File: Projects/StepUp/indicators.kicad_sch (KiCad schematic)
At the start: 10 parts, among them Q5 BSS83P

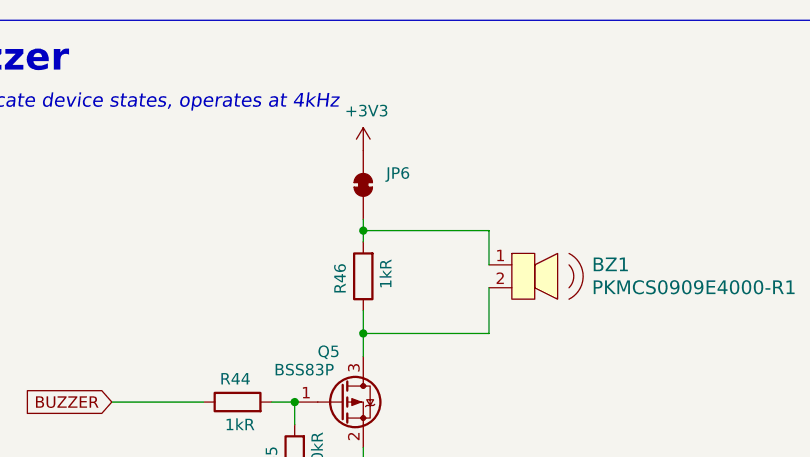
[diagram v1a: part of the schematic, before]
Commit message: feat(layout): DRC ongoing, layout nearly complete
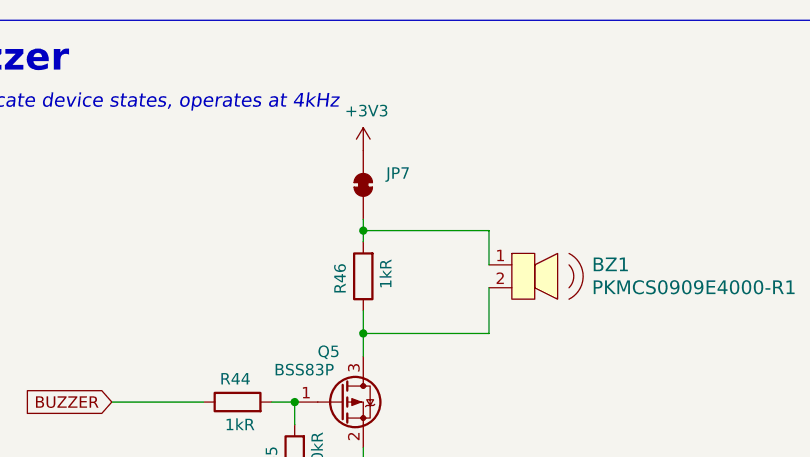
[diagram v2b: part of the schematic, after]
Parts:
- renumbered JP6 to JP7
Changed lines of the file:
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@@
 		(on_board yes)
 		(dnp no)
-		(property "Reference" "#PWR095"
+		(property "Reference" "#PWR0107"
 			(at 71.12 110.49 0)
 			(effects
@@
 			(project "StepUp"
 				(path "/e0cca1c7-c263-49eb-8c40-74000ebe5285/9dda156e-3fdf-45bb-95f8-ac79c3ca0e44"
-					(reference "#PWR095")
+					(reference "#PWR0107")
 					(unit 1)
 				)
@@
 		(on_board yes)
 		(dnp no)
-		(property "Reference" "#PWR097"
+		(property "Reference" "#PWR0109"
 			(at 200.66 77.47 0)
 			(effects
@@
 			(project "StepUp"
 				(path "/e0cca1c7-c263-49eb-8c40-74000ebe5285/9dda156e-3fdf-45bb-95f8-ac79c3ca0e44"
-					(reference "#PWR097")
+					(reference "#PWR0109")
 					(unit 1)
 				)
@@
 		(on_board yes)
 		(dnp no)
-		(property "Reference" "#PWR096"
+		(property "Reference" "#PWR0108"
 			(at 193.04 120.65 0)
 			(effects
@@
 			(project "StepUp"
 				(path "/e0cca1c7-c263-49eb-8c40-74000ebe5285/9dda156e-3fdf-45bb-95f8-ac79c3ca0e44"
-					(reference "#PWR096")
+					(reference "#PWR0108")
 					(unit 1)
 				)
@@
 		(dnp no)
 		(fields_autoplaced yes)
-		(property "Reference" "JP6"
+		(property "Reference" "JP7"
 			(at 203.2 76.1999 90)
 			(effects
@@
 			(project "StepUp"
 				(path "/e0cca1c7-c263-49eb-8c40-74000ebe5285/9dda156e-3fdf-45bb-95f8-ac79c3ca0e44"
-					(reference "JP6")
+					(reference "JP7")
 					(unit 1)
 				)
@@
 		(on_board yes)
 		(dnp no)
-		(property "Reference" "#PWR098"
+		(property "Reference" "#PWR0110"
 			(at 200.66 120.65 0)
 			(effects
@@
 			(project "StepUp"
 				(path "/e0cca1c7-c263-49eb-8c40-74000ebe5285/9dda156e-3fdf-45bb-95f8-ac79c3ca0e44"
-					(reference "#PWR098")
-					(unit 1)
-				)
+					(reference "#PWR0110")
+					(unit 1)
+				)

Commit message: feat(StepUp): Release v0.1
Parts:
- BZ1: MF (none) -> Murata Electronics; Type (none) -> thru-hole
- JP7: now not fitted
- LED2: MPN (none) -> APF3236LSEEZGKQBKC; Manufacturer (none) -> Kingbright; Type (none) -> SMD
- Q5: MPN (none) -> BSS83PH6327XTSA1; Manufacturer (none) -> Infineon Technologies; Type (none) -> SMD
- R43: renamed from R41; Package (none) -> 0603; Tolerance (none) -> 1%; Type (none) -> SMD
- R44: renamed from R42; Package (none) -> 0603; Type (none) -> SMD
- R45: renamed from R43; Package (none) -> 0603; Type (none) -> SMD
- R46: renamed from R44; Package (none) -> 0603; Tolerance (none) -> 1%; Type (none) -> SMD
- R47: renamed from R45; Package (none) -> 0603; Tolerance (none) -> 1%; Type (none) -> SMD
- R48: renamed from R46; Package (none) -> 0603; Tolerance (none) -> 1%; Type (none) -> SMD
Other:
- company: Samio -> SJFOM

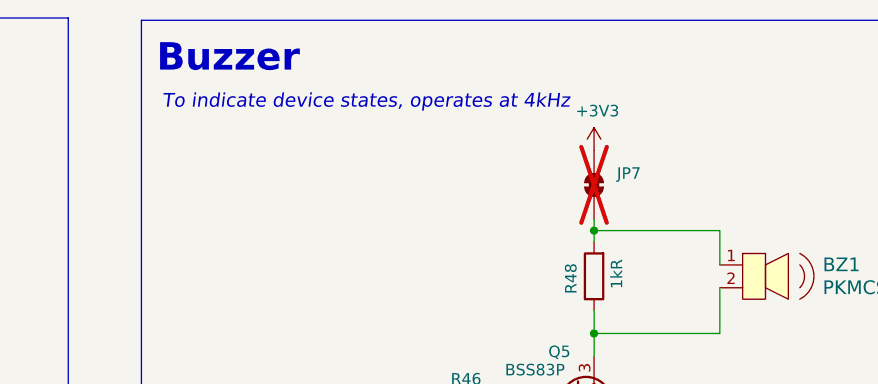
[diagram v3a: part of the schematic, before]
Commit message: feat(outputs): Added STEP file & schematic output
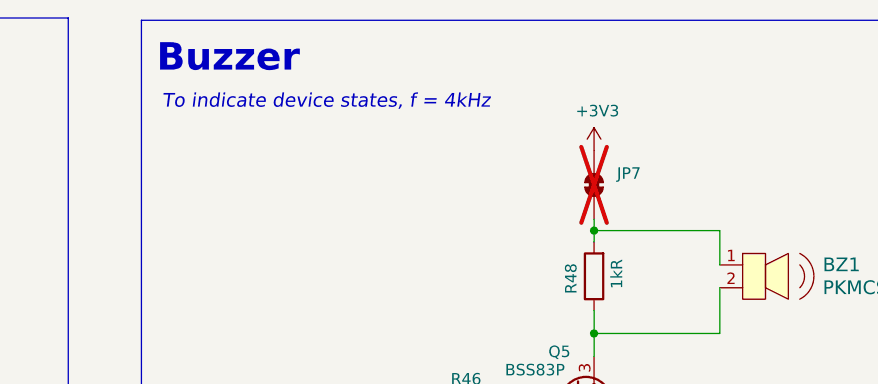
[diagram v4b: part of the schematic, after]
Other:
- note added: "To indicate device states, f = 4kHz"
- note removed: "To indicate device states, operates at 4kHz"
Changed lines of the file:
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@@
 		)
 	)
-	(text "To indicate device states, operates at 4kHz"
+	(text "To indicate device states, f = 4kHz"
 		(exclude_from_sim no)
 		(at 152.654 68.326 0)

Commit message: chore(bom): Update from PCB BoM
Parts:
- R43: MPN (none) -> RC0603FR-07750RL; Manufacturer (none) -> YAGEO; Power (none) -> 0.1W, 1/10W
- R44, R45: MPN (none) -> RC0603JR-07330RL; Manufacturer (none) -> YAGEO; Power (none) -> 0.1W, 1/10W; Tolerance (none) -> 5%
- R46, R48: MPN (none) -> RC0603FR-071KL; Manufacturer (none) -> YAGEO; Power (none) -> 0.1W, 1/10W
- R47: MPN (none) -> RT0603DRE10100KL; Manufacturer (none) -> YAGEO; Power (none) -> 0.1W, 1/10W; Tolerance 1% -> 0.5%
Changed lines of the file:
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@@
 			)
 		)
-		(property "Tolerance" "1%"
+		(property "Tolerance" "0.5%"
 			(at 193.04 107.95 0)
 			(effects
@@
 		)
 		(property "Package" "0603"
+			(at 193.04 107.95 0)
+			(effects
+				(font
+					(size 1.27 1.27)
+				)
+				(hide yes)
+			)
+		)
+		(property "MPN" "RT0603DRE10100KL"
+			(at 193.04 107.95 0)
+			(effects
+				(font
+					(size 1.27 1.27)
+				)
+				(hide yes)
+			)
+		)
+		(property "Manufacturer" "YAGEO"
+			(at 193.04 107.95 0)
+			(effects
+				(font
+					(size 1.27 1.27)
+				)
+				(hide yes)
+			)
+		)
+		(property "Power" "0.1W, 1/10W"
 			(at 193.04 107.95 0)
 			(effects
@@
 			)
 		)
+		(property "MPN" "RC0603JR-07330RL"
+			(at 102.87 91.44 0)
+			(effects
+				(font
+					(size 1.27 1.27)
+				)
+				(hide yes)
+			)
+		)
+		(property "Manufacturer" "YAGEO"
+			(at 102.87 91.44 0)
+			(effects
+				(font
+					(size 1.27 1.27)
+				)
+				(hide yes)
+			)
+		)
+		(property "Power" "0.1W, 1/10W"
+			(at 102.87 91.44 0)
+			(effects
+				(font
+					(size 1.27 1.27)
+				)
+				(hide yes)
+			)
+		)
+		(property "Tolerance" "5%"
+			(at 102.87 91.44 0)
+			(effects
+				(font
+					(size 1.27 1.27)
+				)
+				(hide yes)
+			)
+		)
 		(pin "1"
 		)
@@
 			)
 		)
+		(property "MPN" "RC0603FR-07750RL"
+			(at 102.87 83.82 0)
+			(effects
+				(font
+					(size 1.27 1.27)
+				)
+				(hide yes)
+			)
+		)
+		(property "Manufacturer" "YAGEO"
+			(at 102.87 83.82 0)
+			(effects
+				(font
+					(size 1.27 1.27)
+				)
+				(hide yes)
+			)
+		)
+		(property "Power" "0.1W, 1/10W"
+			(at 102.87 83.82 0)
+			(effects
+				(font
+					(size 1.27 1.27)
+				)
+				(hide yes)
+			)
+		)
 		(pin "1"
 		)
@@
 		)
 		(property "Package" "0603"
+			(at 200.66 87.63 0)
+			(effects
+				(font
+					(size 1.27 1.27)
+				)
+				(hide yes)
+			)
+		)
+		(property "MPN" "RC0603FR-071KL"
+			(at 200.66 87.63 0)
+			(effects
+				(font
+					(size 1.27 1.27)
+				)
+				(hide yes)
+			)
+		)
+		(property "Manufacturer" "YAGEO"
+			(at 200.66 87.63 0)
+			(effects
+				(font
+					(size 1.27 1.27)
+				)
+				(hide yes)
+			)
+		)
+		(property "Power" "0.1W, 1/10W"
 			(at 200.66 87.63 0)
 			(effects
@@
 			)
 		)
+		(property "MPN" "RC0603FR-071KL"
+			(at 186.69 101.6 0)
+			(effects
+				(font
+					(size 1.27 1.27)
+				)
+				(hide yes)
+			)
+		)
+		(property "Manufacturer" "YAGEO"
+			(at 186.69 101.6 0)
+			(effects
+				(font
+					(size 1.27 1.27)
+				)
+				(hide yes)
+			)
+		)
+		(property "Power" "0.1W, 1/10W"
+			(at 186.69 101.6 0)
+			(effects
+				(font
+					(size 1.27 1.27)
+				)
+				(hide yes)
+			)
+		)
 		(pin "1"
 		)
@@
 			(at 102.87 99.06 0)
 			(effects
+				(font
+					(size 1.27 1.27)
+				)
+				(hide yes)
+			)
+		)
+		(property "MPN" "RC0603JR-07330RL"
+			(at 102.87 99.06 0)
+			(effects
+				(font
+					(size 1.27 1.27)
+				)
+				(hide yes)
+			)
+		)
+		(property "Manufacturer" "YAGEO"
+			(at 102.87 99.06 0)
+			(effects
+				(font
+					(size 1.27 1.27)
+				)
+				(hide yes)
+			)
+		)
+		(property "Power" "0.1W, 1/10W"
+			(at 102.87 99.06 0)
+			(effects
+				(font
+					(size 1.27 1.27)
+				)
+				(hide yes)
+			)
+		)
+		(property "Tolerance" "5%"
+			(at 102.87 99.06 0)
+			(effects

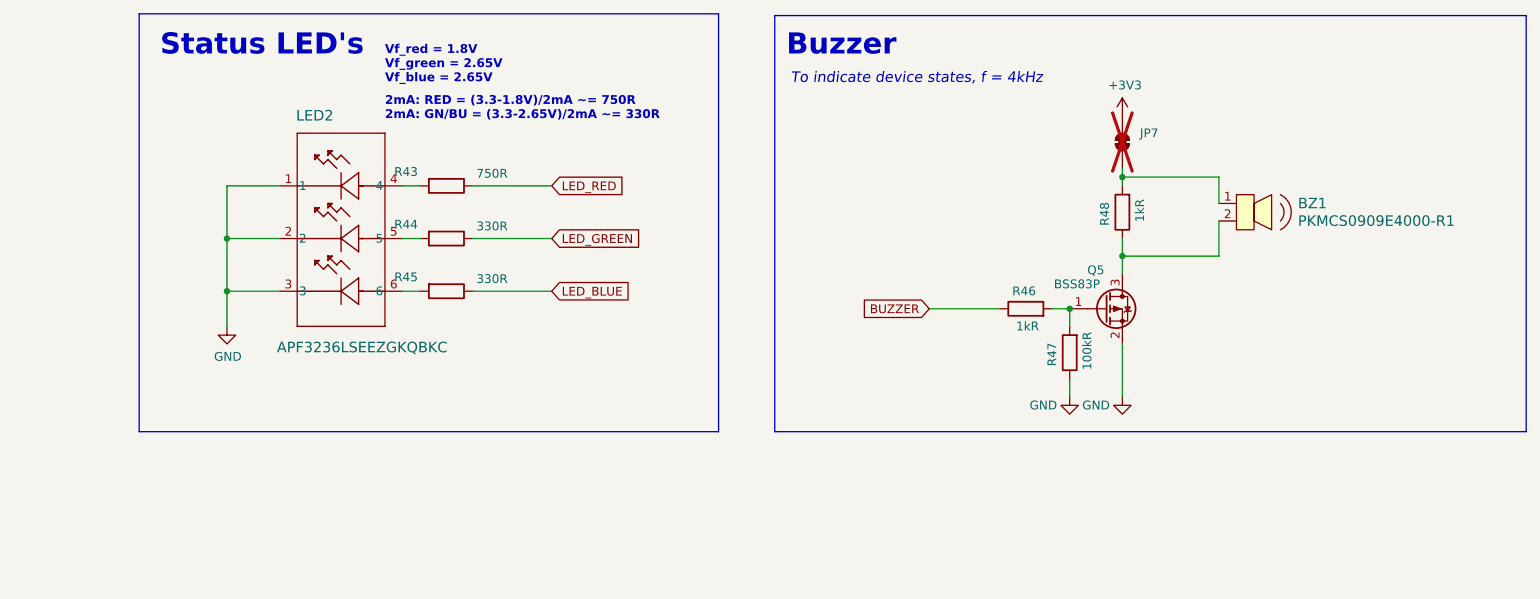
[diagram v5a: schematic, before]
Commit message: feat(v0.2): Schematic updated, PCB layout start
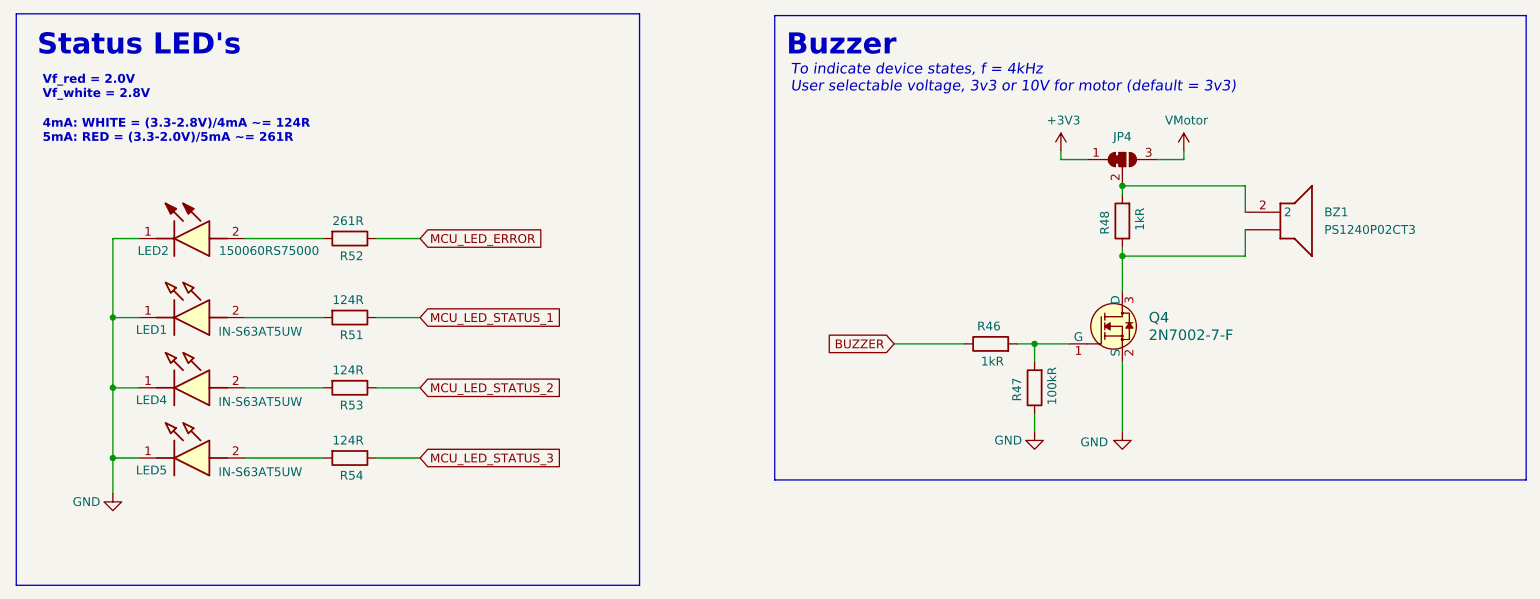
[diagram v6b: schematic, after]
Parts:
- removed BZ1: PKMCS0909E4000-R1, digikey-footprints:Piezo_9x9mm_PKMCS0909E4000-R1, symbol dk_Alarms-Buzzers-and-Sirens:PKMCS0909E4000-R1
- removed JP7: SolderJumper_2_Bridged, Jumper:SolderJumper-2_P1.3mm_Bridged2Bar_RoundedPad1.0x1.5mm, symbol Jumper:SolderJumper_2_Bridged
- removed LED2: APF3236LSEEZGKQBKC, Snapeda:APF3236LSEEZGKQBKC_KNB, symbol Snapeda_kicad_2:APF3236LSEEZGKQBKC
- removed Q5: BSS83P, Package_TO_SOT_SMD:SOT-23, symbol Transistor_FET:BSS83P
- removed R43: 750R, Resistor_SMD:R_0603_1608Metric, symbol Device:R
- removed R44, R45: 330R, Resistor_SMD:R_0603_1608Metric, symbol Device:R
- added BZ1: PS1240P02CT3, Samacsys:PS1240P02BT, symbol Samacsys:PS1240P02CT3
- added JP4: SolderJumper_3_Bridged12, Jumper:SolderJumper-3_P1.3mm_Bridged12_RoundedPad1.0x1.5mm, symbol Jumper:SolderJumper_3_Bridged12
- added LED1, LED4, LED5: IN-S63AT5UW, Samacsys:INS63AT5UW, symbol Samacsys:IN-S63AT5UW
- added LED2: 150060RS75000, Samacsys:LEDC1608X80N, symbol Samacsys:150060RS75000
- added Q4: 2N7002-7-F, digikey-footprints:SOT-23-3, symbol dk_Transistors-FETs-MOSFETs-Single:2N7002-7-F
- added R51, R53, R54: 124R, Resistor_SMD:R_0603_1608Metric, symbol Device:R
- added R52: 261R, Resistor_SMD:R_0603_1608Metric, symbol Device:R
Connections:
- net +3V3: now also JP4.1 (A)
- net GND: now also LED1.1 (K), LED2.1 (K), LED4.1 (K), LED5.1 (K), Q4.2 (S)
- net at R46.2, R47.2: now also Q4.1 (G)
- net at R48.1: now also BZ1., Q4.3 (D)
- net at R48.2: now also BZ1.2, JP4.2 (C)
- new net: LED2.2 (A), R52.2
- new net: LED5.2 (A), R54.2
- new net: LED4.2 (A), R53.2
- new net: LED1.2 (A), R51.2
- new net MCU_LED_ERROR: R52.1
- new net MCU_LED_STATUS_1: R51.1
- new net MCU_LED_STATUS_2: R53.1
- new net MCU_LED_STATUS_3: R54.1
- new net VMotor: JP4.3 (B)
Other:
- note added: "4mA: WHITE = (3.3-2.8V)/4mA ~= 124R 5mA: RED = (3.3-2.0V)/5mA ~= 261R"
- note added: "To indicate device states, f = 4kHz User selectable voltage, 3v3 or 10V for motor (default = 3v3)"
- note added: "Vf_red = 2.0V Vf_white = 2.8V"
- note removed: "2mA: RED = (3.3-1.8V)/2mA ~= 750R 2mA: GN/BU = (3.3-2.65V)/2mA ~= 330R"
- note removed: "To indicate device states, f = 4kHz"
- note removed: "Vf_red = 1.8V Vf_green = 2.65V Vf_blue = 2.65V"
- moved on the sheet: R46, R47, R48

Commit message: feat(v0.2): Rough layout begins
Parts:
- removed LED1, LED4, LED5: IN-S63AT5UW, Samacsys:INS63AT5UW, symbol Samacsys:IN-S63AT5UW
- removed LED2: 150060RS75000, Samacsys:LEDC1608X80N, symbol Samacsys:150060RS75000
- removed R53, R54: 124R, Resistor_SMD:R_0603_1608Metric, symbol Device:R
- added LED2: IN-S63ASR, Samacsys:LEDC1706X110N, symbol Samacsys:IN-S63ASR
- added LED3, LED4, LED5: IN-S63AS5UW, Samacsys:INS63AS5UW, symbol Samacsys:IN-S63AS5UW
- added R50, R52: 100R, Resistor_SMD:R_0603_1608Metric, symbol Device:R
- R49: renamed from R52; value 261R -> 220R; MPN ERJ-3EKF2610V -> (none); Manufacturer Panasonic Electronic Components -> (none)
- R51: value 124R -> 100R; MPN ERJ-3EKF1240V -> RC0603FR-07100RL; Manufacturer Panasonic Electronic Components -> YAGEO; Package 0603 -> 0603
- renumbered JP4 to JP2, Q4 to Q7, R46 to R53, R47 to R54, R48 to R55
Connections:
- net GND: now also LED2.1 (K), LED3.1 (K), LED4.1 (K), LED5.1 (K)
- net MCU_LED_STATUS_1: now also R50.2; no longer R51.1
- net MCU_LED_STATUS_2: now also R51.2
- net MCU_LED_STATUS_3: now also R52.2
- net at R49.2: now also LED2.2 (A)
- net at Q7.3 (D), R55.1: now also BZ1.1; no longer BZ1.
- new net: LED3.2 (A), R50.1
- new net: LED4.2 (A), R51.1
- new net: LED5.2 (A), R52.1
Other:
- note added: "4mA: WHITE = (3.3-2.8V)/4mA = 100R 5mA: RED = (3.3-2.0V)/5mA ~= 220R"
- note added: "LED power calculations"
- note added: "Status LEDs, surface-mount, side-entry, clear"
- note added: "Vf_red = 2.2V Vf_white = 2.9V"
- note removed: "4mA: WHITE = (3.3-2.8V)/4mA ~= 124R 5mA: RED = (3.3-2.0V)/5mA ~= 261R"
- note removed: "Vf_red = 2.0V Vf_white = 2.8V"
- moved on the sheet: R49

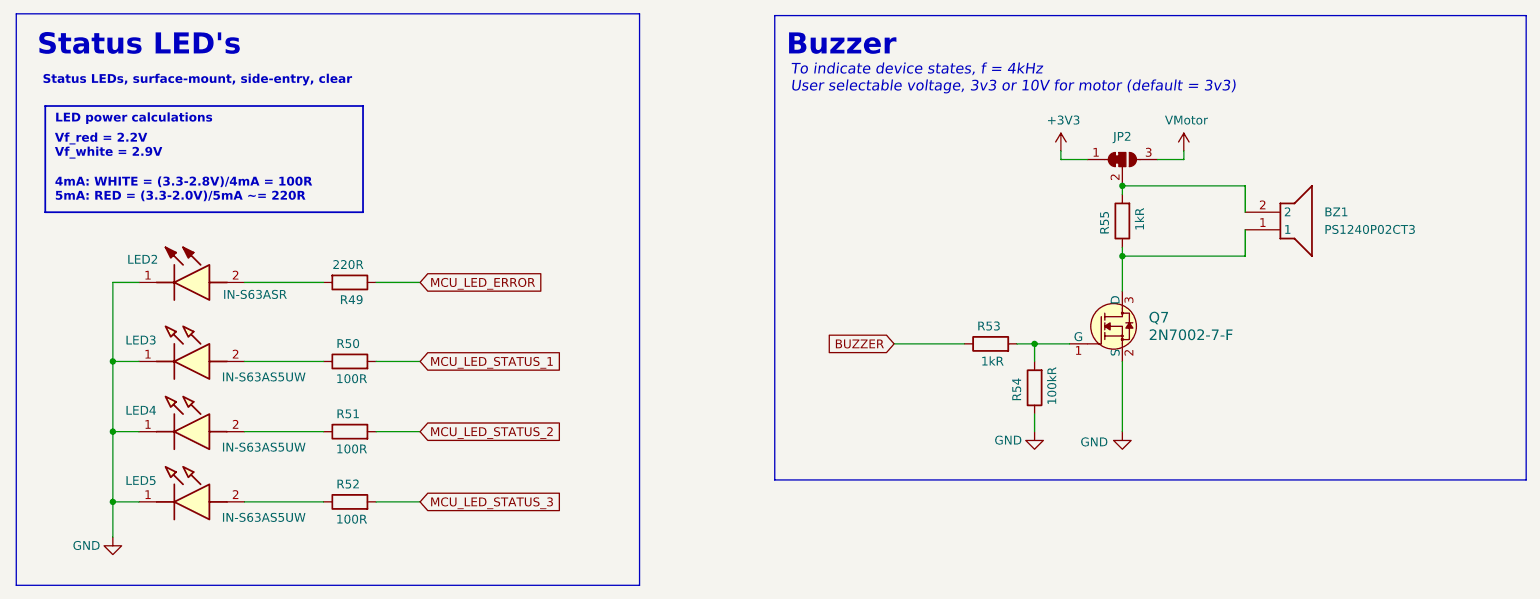
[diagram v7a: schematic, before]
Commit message: feat(v0.2): Component layout from CAD
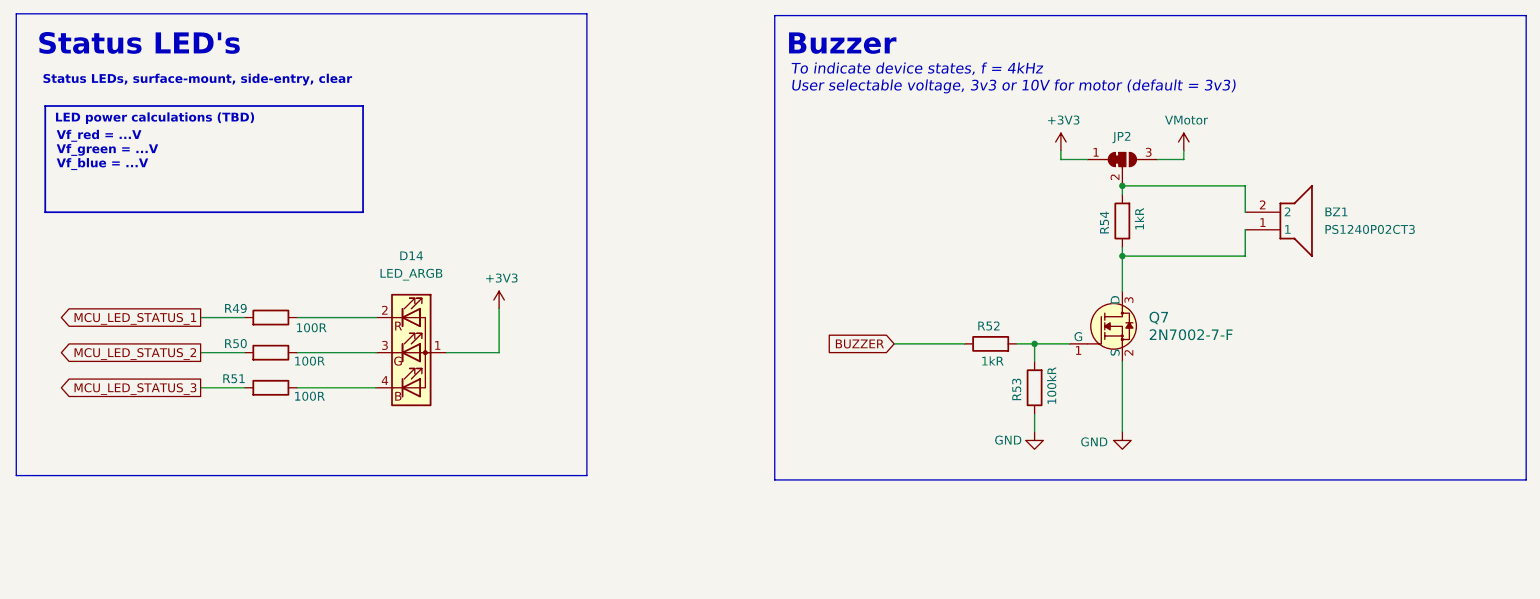
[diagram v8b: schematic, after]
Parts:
- removed LED2: IN-S63ASR, Samacsys:LEDC1706X110N, symbol Samacsys:IN-S63ASR
- removed LED3, LED4, LED5: IN-S63AS5UW, Samacsys:INS63AS5UW, symbol Samacsys:IN-S63AS5UW
- removed R49: 220R, Resistor_SMD:R_0603_1608Metric, symbol Device:R
- added D14: LED_ARGB, LED_THT:LED_D5.0mm-4_RGB, symbol Device:LED_ARGB
- BZ1: now left out of the parts list
- renumbered R50 to R49, R51 to R50, R52 to R51, R53 to R52, R54 to R53, R55 to R54
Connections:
- net +3V3: now also D14.1 (A)
- net at R49.1: now also D14.2 (RK)
- net at R50.1: now also D14.3 (GK)
- net at R51.1: now also D14.4 (BK)
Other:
- note added: "LED power calculations (TBD)"
- note added: "Vf_red = ...V Vf_green = ...V Vf_blue = ...V"
- note removed: "4mA: WHITE = (3.3-2.8V)/4mA = 100R 5mA: RED = (3.3-2.0V)/5mA ~= 220R"
- note removed: "LED power calculations"
- note removed: "Vf_red = 2.2V Vf_white = 2.9V"
- moved on the sheet: R49, R50, R51
